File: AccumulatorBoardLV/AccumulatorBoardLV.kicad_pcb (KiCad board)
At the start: 2 copper layers, 47 parts, among them J1 Contactor 1, J10 To HV Board, J11 IMD Reset, J12 TS Interlock, J13 Temp Reset, J14 To ECU, J15 Charger LV, J16 Charger Interlock, J17 Lid Interlock, J18 From HV Board, J19 Chip 1, J2 BMS Connector 1, J20 Chip 2, J21 Chip 3, J22 Chip 4, J3 BMS Connector 2, J4 BMS TX, J5 BMS RX, J6 Current Sensor, J7 Contactor 2, J8 IMD LV, J9 BMS Reset, U1 DE1A1B-L2-12V, U10 MCP3008, U11 ISO1050, U12 stm_nucleo_FK303K8, U13 MCP3008, U14 MCP3008, U2 LM555N, U3 SN754410, U4 DE1A1B-L2-12V, U5 L78S05CV-DG, U6 DE1A1B-L2-12V, U7 DK1A1B-12V, U8 ADUM4154ARIZ, U9 MCP3008

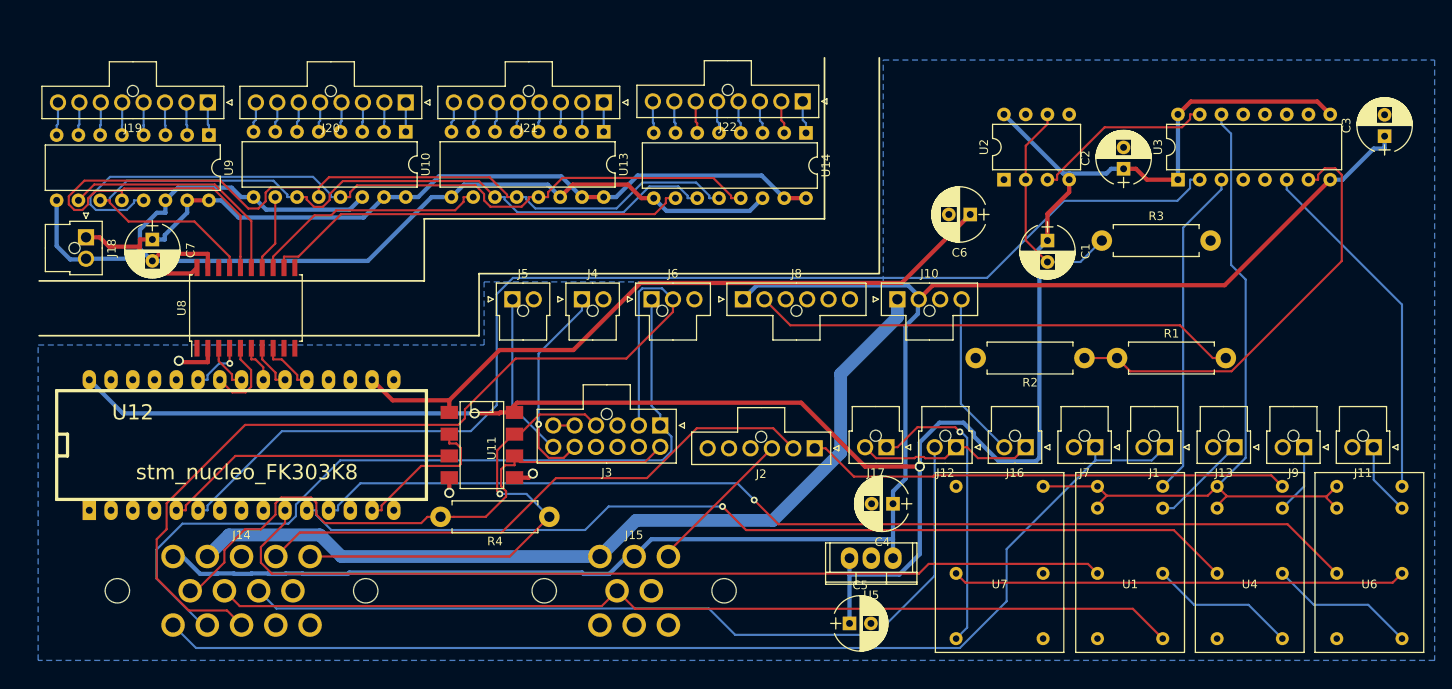
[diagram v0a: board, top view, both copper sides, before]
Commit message: Re-layout Accumulator LV PCB, adding mounting holes
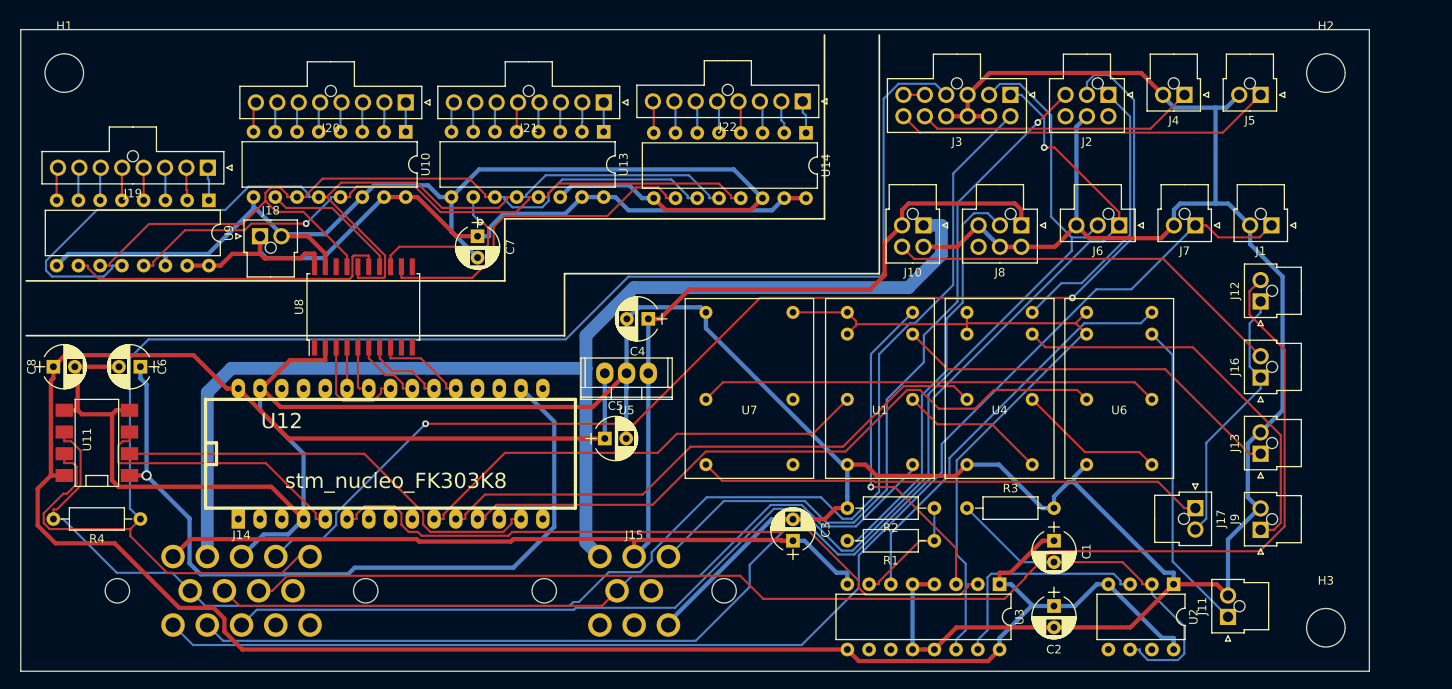
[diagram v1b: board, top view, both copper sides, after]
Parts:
- added C8: CP, Capacitors_THT:CP_Radial_D5.0mm_P2.50mm, F.Cu at (44.1, 122.4)
- added H1: MtngHole, Mounting_Holes:MountingHole_4.5mm, F.Cu at (45.3, 88.1)
- added H2: MtngHole, Mounting_Holes:MountingHole_4.5mm, F.Cu at (192.7, 88.1)
- added H3: MtngHole, Mounting_Holes:MountingHole_4.5mm, F.Cu at (192.7, 152.9)
- C1, C2, C3, C4, C5, C7: footprint Capacitors_THT:CP_Radial_D6.3mm_P2.50mm -> Capacitors_THT:CP_Radial_D5.0mm_P2.50mm
- C6: value C -> CP; footprint Capacitors_THT:CP_Radial_D6.3mm_P2.50mm -> Capacitors_THT:CP_Radial_D5.0mm_P2.50mm
- J10: footprint Connectors_Molex:Molex_NanoFit_1x04x2.50mm_Straight -> Connectors_Molex:Molex_NanoFit_2x02x2.50mm_Straight
- J2, J8: footprint Connectors_Molex:Molex_NanoFit_1x06x2.50mm_Straight -> Connectors_Molex:Molex_NanoFit_2x03x2.50mm_Straight
- R1, R2, R3, R4: footprint Resistors_THT:R_Axial_DIN0411_L9.9mm_D3.6mm_P12.70mm_Horizontal -> Resistors_THT:R_Axial_DIN0207_L6.3mm_D2.5mm_P10.16mm_Horizontal
- moved C6 98.5 mm to (54.2, 122.4)
- moved J5 90.6 mm to (185.0, 90.7), turned to 180 degrees
- moved C3 83.7 mm to (130.4, 142.7)
- moved J4 74.3 mm to (176.1, 90.7), turned to 180 degrees
- moved J3 56.2 mm to (155.8, 90.7)
- moved J6 55.3 mm to (168.5, 105.9), turned to 180 degrees
- moved J2 53.7 mm to (167.3, 90.7)
- moved C2 51.7 mm to (160.9, 150.4), turned to 270 degrees
- moved U3 51.6 mm to (154.6, 147.8), turned to 270 degrees
- moved U2 51.2 mm to (174.9, 147.8), turned to 270 degrees
- moved R4 47.8 mm to (54.2, 140.2)
- moved U11 45.0 mm to (49.1, 131.3), turned to 90 degrees
- moved J12 39.4 mm to (185.0, 114.8), turned to 90 degrees
- moved C7 38.0 mm to (93.6, 107.2)
- moved J17 36.8 mm to (177.4, 138.9), turned to 270 degrees
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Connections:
- J14 pad 13: Net-(J14-Pad13) -> (no net)
- J14 pad 14: Net-(J14-Pad14) -> (no net)
- J14 pad 9: Net-(J14-Pad9) -> (no net)
- J15 pad 5: /AIRS_FINAL_OUT_CHARGER -> (no net)
- J15 pad 6: /CHARGER_CONTROL -> (no net)
- J15 pad 7: Net-(J15-Pad7) -> (no net)
- J2 pad 4: /CHARGE_CONTROL -> (no net)
- J2 pad 6: Net-(J2-Pad6) -> (no net)
- J8 pad 6: Net-(J8-Pad6) -> (no net)
- U12 pad 1: Net-(U12-Pad1) -> (no net)
- U12 pad 13: Net-(U12-Pad13) -> (no net)
- U12 pad 15: Net-(U12-Pad15) -> (no net)
- U12 pad 16: Net-(U12-Pad16) -> (no net)
- U12 pad 18: Net-(U12-Pad18) -> (no net)
- U12 pad 19: Net-(U12-Pad19) -> (no net)
- U12 pad 2: Net-(U12-Pad2) -> (no net)
- U12 pad 26: Net-(U12-Pad26) -> (no net)
- U12 pad 27: Net-(U12-Pad27) -> (no net)
- U12 pad 28: Net-(U12-Pad28) -> (no net)
- U12 pad 3: Net-(U12-Pad3) -> (no net)
- U12 pad 7: Net-(U12-Pad7) -> (no net)
- U12 pad 8: Net-(U12-Pad8) -> (no net)
- U12 pad 9: Net-(U12-Pad9) -> (no net)
- U2 pad 5: Net-(U2-Pad5) -> (no net)
- U2 pad 7: Net-(U2-Pad7) -> (no net)
- U3 pad 10: Net-(U3-Pad10) -> (no net)
- U3 pad 11: Net-(U3-Pad11) -> (no net)
- U7 pad 5: Net-(U7-Pad5) -> (no net)
- U7 pad 6: Net-(U7-Pad6) -> (no net)
- U8 pad 1: /3.3V -> (no net)
- U8 pad 10: Net-(U8-Pad10) -> (no net)
- U8 pad 11: Net-(U8-Pad11) -> (no net)
- U8 pad 18: /TEMP_SCLK -> (no net)
- U8 pad 9: Net-(U8-Pad9) -> (no net)
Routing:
- net GND: track 9.20 -> 477.1 mm, vias 3 -> 0
- net /CAN_H: track 55.9 -> 188.0 mm, vias 1 -> 0
- net /CAN_L: track 70.7 -> 172.3 mm
- net /V_L: track 67.6 -> 141.0 mm, vias 0 -> 2
- net /V_S: track 17.6 -> 85.6 mm, vias 0 -> 1
- net /5V_BMS: track 95.9 -> 158.4 mm, vias 0 -> 1
- net /TEMP_FLT: track 141.5 -> 81.4 mm
- net /AIRS_ACC_OUT: track 98.9 -> 156.2 mm
- net /TEMP_FLT_LATCHED: track 106.4 -> 54.4 mm
- net /BMS_FLT_LATCHED: track 111.9 -> 67.1 mm, vias 1 -> 0
- net /IMD_FLT_LATCHED: track 123.7 -> 79.9 mm, vias 1 -> 0
- net /SIG_CURRENT: track 112.2 -> 154.4 mm
- net /12V_SRC: track 101.7 -> 142.0 mm
- net /BMS_RESET: track 8.16 -> 46.8 mm
- net /IMD_FLT_5: track 51.2 -> 13.7 mm
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- removed copper zone on B.Cu, net GND
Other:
- board outline added: 157.5 x 74.9 mm
- net class Default: via_drill 0.6 -> 0.4
- net class Ground added: clearance 0.3, trace_width 0.5, via_dia 1.2, via_drill 0.8
- net class MainPower: clearance 0.4 -> 0.3

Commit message: Add planes to Accumulator LV board
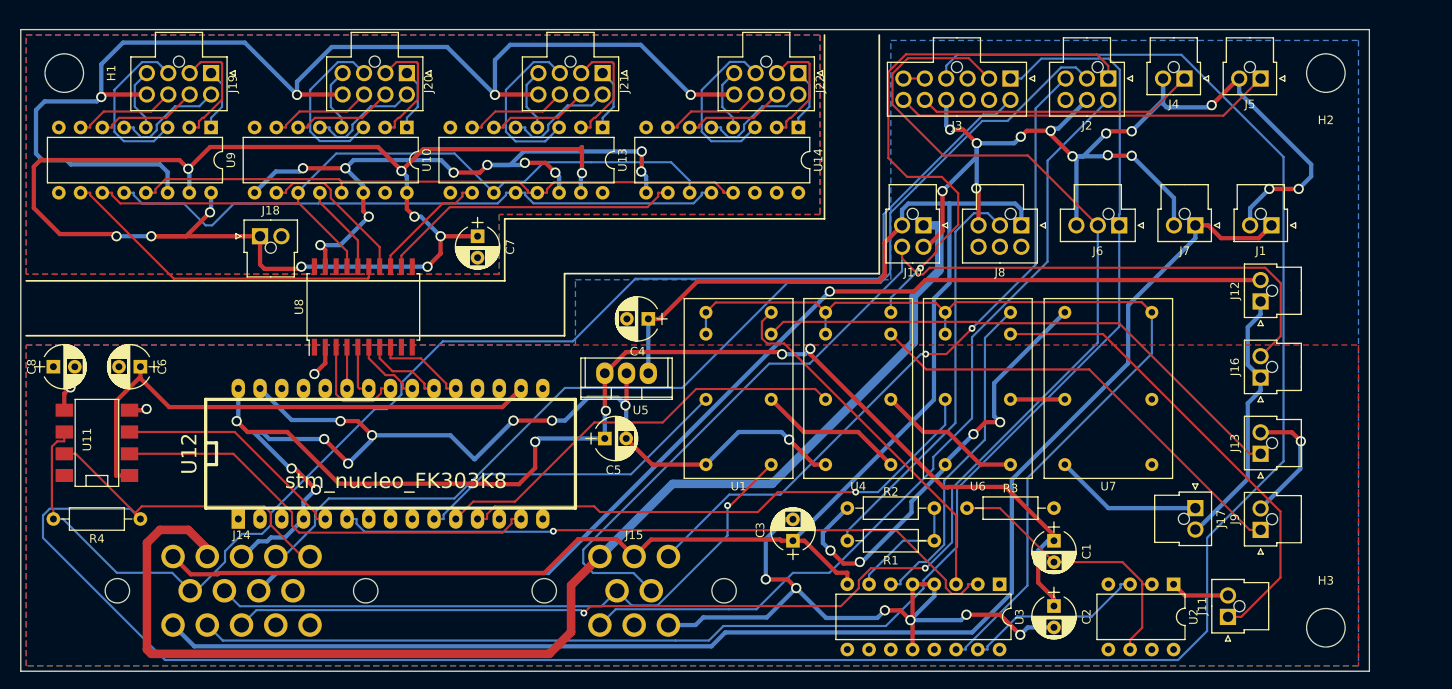
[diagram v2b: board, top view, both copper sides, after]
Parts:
- J19, J20, J21, J22: footprint Connectors_Molex:Molex_NanoFit_1x08x2.50mm_Straight -> Connectors_Molex:Molex_NanoFit_2x04x2.50mm_Straight
- moved U7 41.9 mm to (167.3, 126.2)
- moved U1 16.5 mm to (120.3, 126.2)
- moved U4 16.5 mm to (134.2, 126.2)
- moved U6 16.5 mm to (148.2, 126.2)
- moved J19 11.1 mm to (62.5, 88.1)
- moved U9 8.51 mm to (62.5, 94.5)
- moved J21 3.43 mm to (108.2, 88.1)
- moved J20 3.43 mm to (85.3, 88.1)
- moved J22 3.34 mm to (131.1, 88.1)
- moved J2 1.91 mm to (167.3, 88.8)
- moved J3 1.91 mm to (155.8, 88.8)
- moved J4 1.91 mm to (176.1, 88.8)
- moved J5 1.91 mm to (185.0, 88.8)
- moved U14 1.09 mm to (131.1, 94.5)
- moved U13 0.52 mm to (108.2, 94.5)
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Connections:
- net Net-(U1-Pad6) renamed /AIRS_TEMP_OUT
- net Net-(U4-Pad6) renamed /AIRS_BMS_OUT
- net Net-(U6-Pad6) renamed /AIRS_IMD_OUT
- J12 pad 1: /AIRS_RELAYS_OUT -> /AIRS_LID_OUT
- J15 pad 5: (no net) -> /AIRS_FINAL_CHARGER
- J15 pad 6: (no net) -> /CHARGER_CONTROL
- J16 pad 1: /AIRS_RELAYS_OUT -> /AIRS_LID_OUT
- J17 pad 1: Net-(J17-Pad1) -> /AIRS_RELAYS_OUT
- J17 pad 2: /AIRS_RELAYS_OUT -> /AIRS_LID_OUT
- J19 pad 8: Net-(J19-Pad8) -> /BATT-
- J2 pad 4: (no net) -> /CHARGER_CONTROL
- J20 pad 8: Net-(J20-Pad8) -> /BATT-
- J21 pad 8: Net-(J21-Pad8) -> /BATT-
- J22 pad 8: Net-(J22-Pad8) -> /BATT-
- U10 pad 8: Net-(J20-Pad8) -> (no net)
- U13 pad 8: Net-(J21-Pad8) -> (no net)
- U14 pad 8: Net-(J22-Pad8) -> (no net)
- U7 pad 4: Net-(J17-Pad1) -> /AIRS_RELAYS_OUT
- U9 pad 8: Net-(J19-Pad8) -> (no net)
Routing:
- net +5V: track 260.1 -> 135.2 mm, vias 0 -> 6
- net /CAN_H: track 188.0 -> 299.6 mm
- net /CHARGER_CONTROL: track 0.00 -> 98.0 mm
- net /BATT-: track 136.8 -> 223.1 mm, vias 0 -> 14
- net /AIRS_FINAL_CHARGER: track 47.2 -> 121.3 mm
- net /3.3V_TS: track 93.9 -> 161.0 mm, vias 0 -> 10
- net GND: track 477.1 -> 417.2 mm, vias 0 -> 38
- net Net-(J17-Pad1): track 59.3 -> 0.00 mm
- net /AIRS_IMD_OUT: track 53.7 -> 6.35 mm
- net /BMS_FLT: track 32.6 -> 65.9 mm, vias 0 -> 1
- net /AIRS_LID_OUT: track 0.00 -> 31.2 mm
- net /TEMP_SSO: track 115.5 -> 85.1 mm
- net +3V3: track 90.5 -> 62.3 mm, vias 1 -> 0
- net /TIMER_H: track 85.8 -> 112.1 mm
- net +12V: track 167.7 -> 193.7 mm
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- added copper zone on F.Cu, net +5V
- added copper zone on F.Cu, net /3.3V_TS
- added copper zone on B.Cu, net /BATT-
- added copper zone on B.Cu, net GND
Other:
- net class HighSpeed added: clearance 0.2, trace_width 0.25, via_dia 100, via_drill 50
- net class Power: trace_width 1.5 -> 1; via_dia 3.6 -> 2.4; via_drill 2.4 -> 1.6

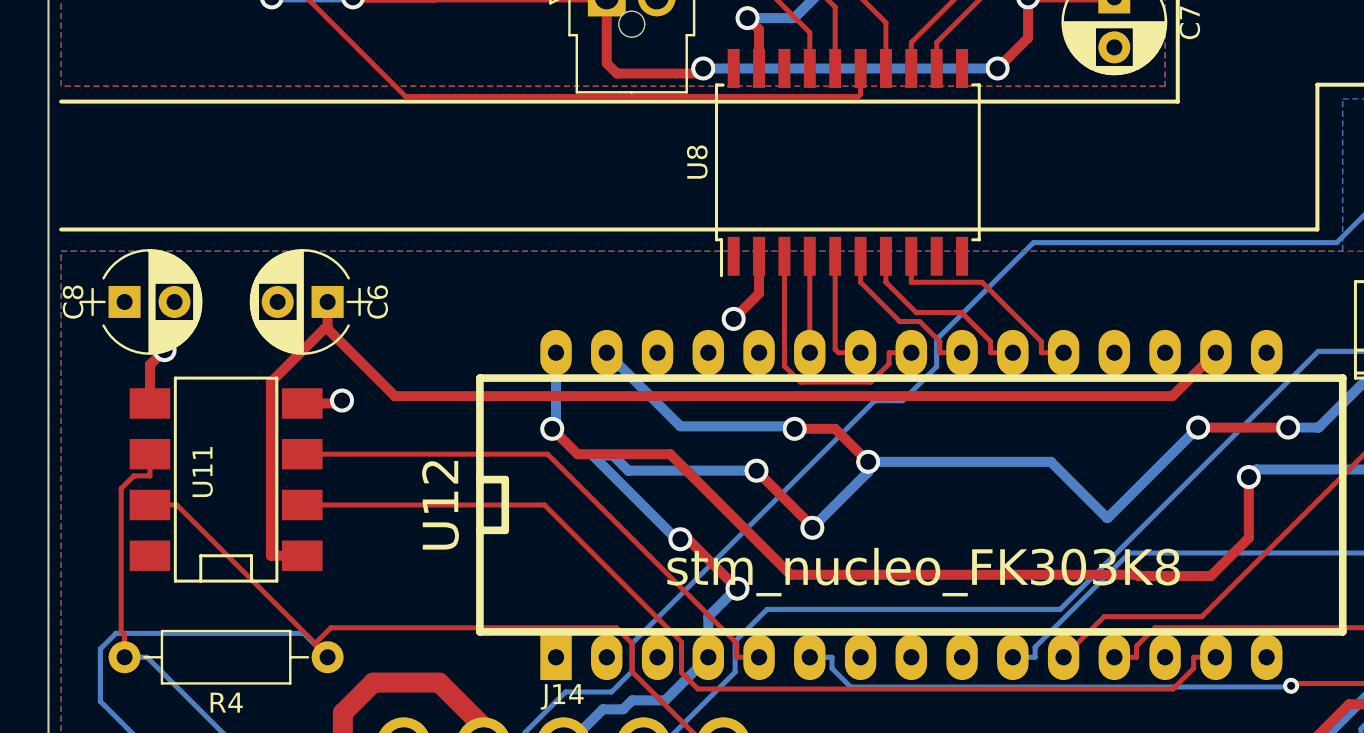
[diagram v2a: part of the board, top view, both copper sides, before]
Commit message: Create joined PCBs for manufacturing on the same board
Accumulator one is having problems with the exported files on DFM for some reason
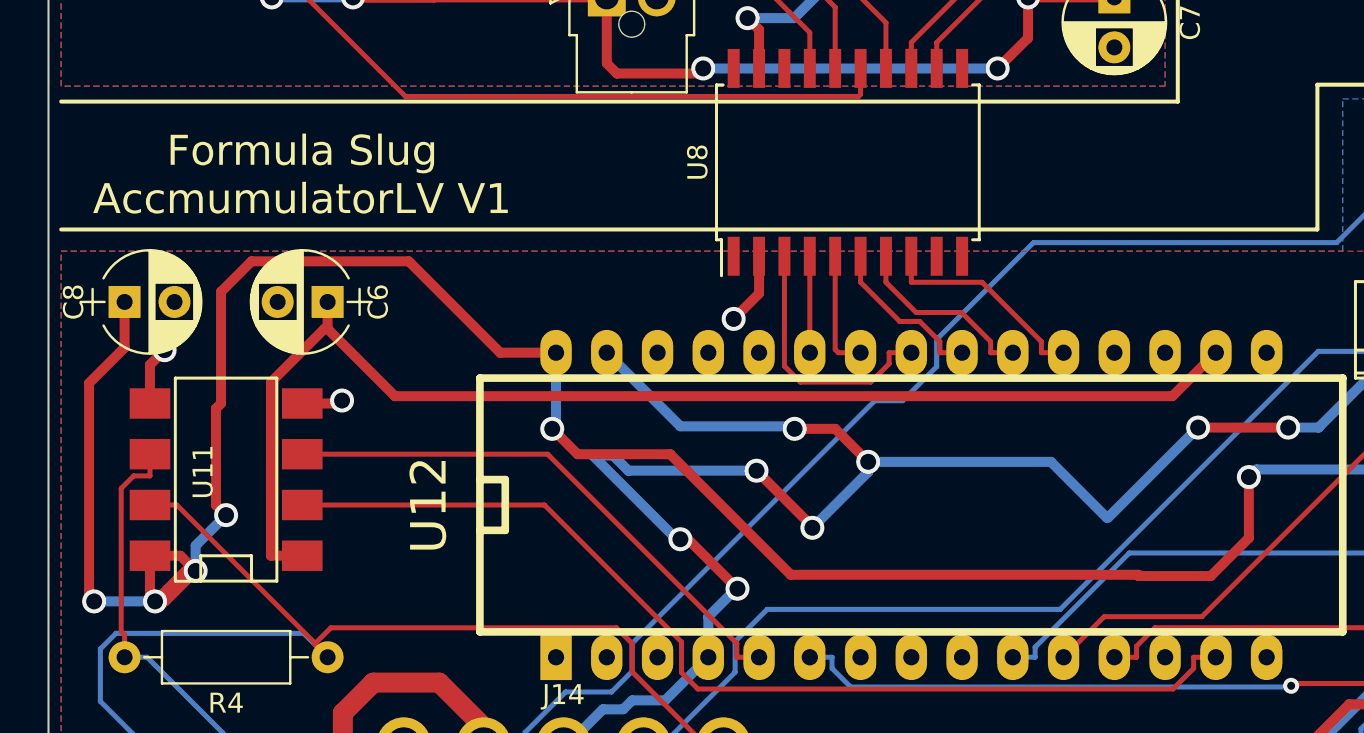
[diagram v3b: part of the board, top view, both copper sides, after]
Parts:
- U12: footprint arduino:arduino_mini -> FSFootprints:arduino_mini
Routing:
- net +5V: track 135.2 -> 198.7 mm, vias 6 -> 10
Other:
- board text added: "Formula Slug AccmumulatorLV V1"

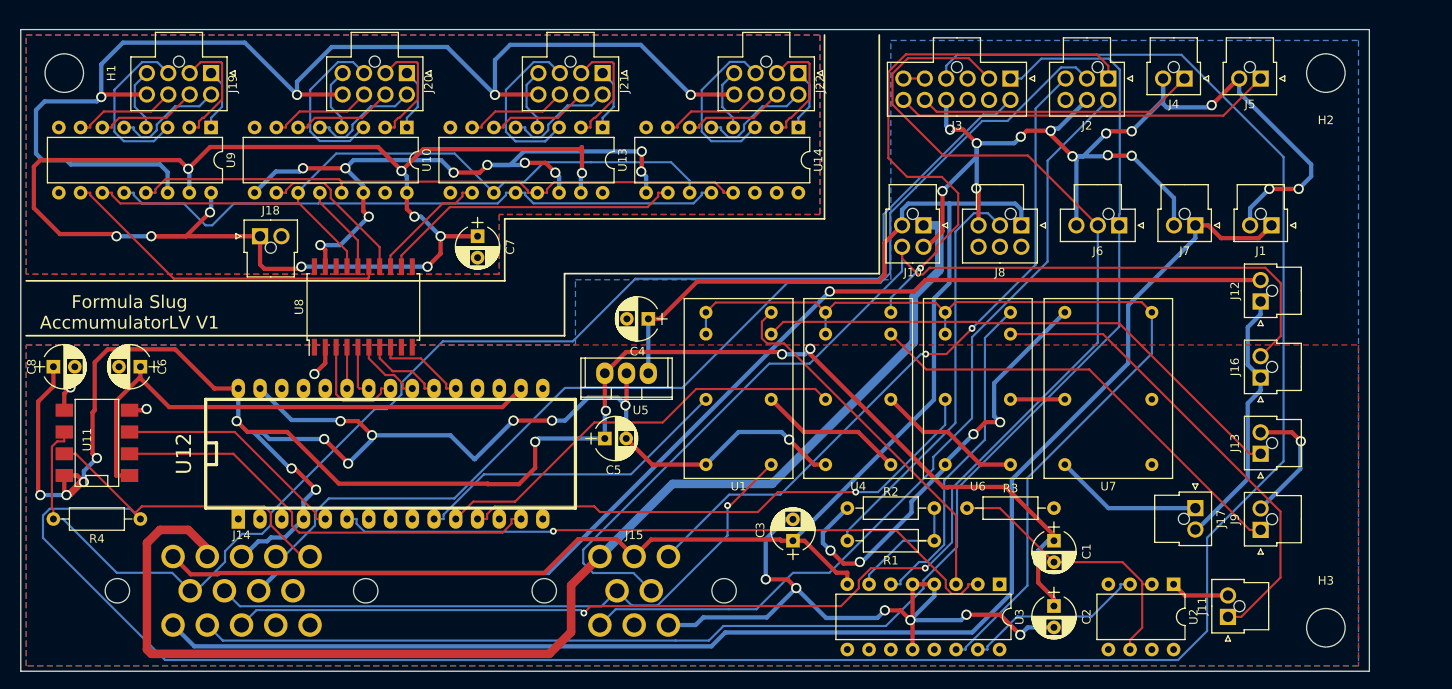
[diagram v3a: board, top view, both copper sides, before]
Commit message: Tweak routing on boards, add mounting holes to dash switchbox
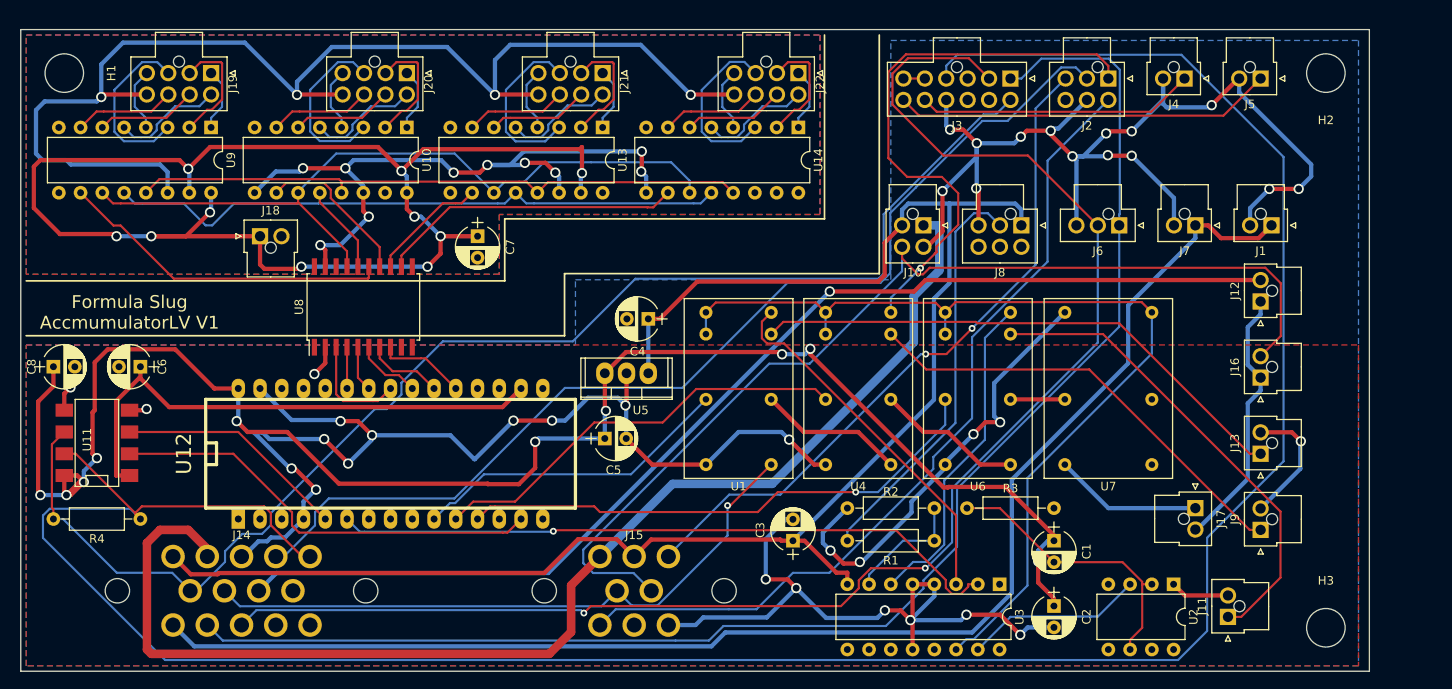
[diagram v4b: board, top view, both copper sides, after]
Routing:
- net /SCLK: track 73.0 -> 72.2 mm
- net /TEMP_SSO: track 85.1 -> 84.5 mm
- net Net-(U12-Pad24): track 6.00 -> 5.35 mm
